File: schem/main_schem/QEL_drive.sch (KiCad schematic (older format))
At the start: 7 parts, among them P1 CONN_2, Q1 ENHANCED_MOSFET_N, U1 PS2501-2

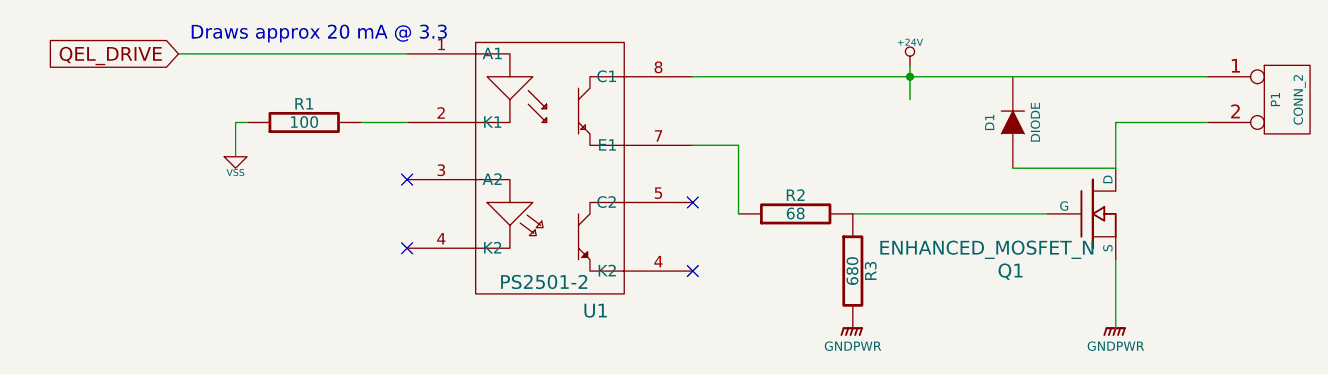
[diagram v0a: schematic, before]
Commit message: Begin board, layout mcu, xtal, eeprom
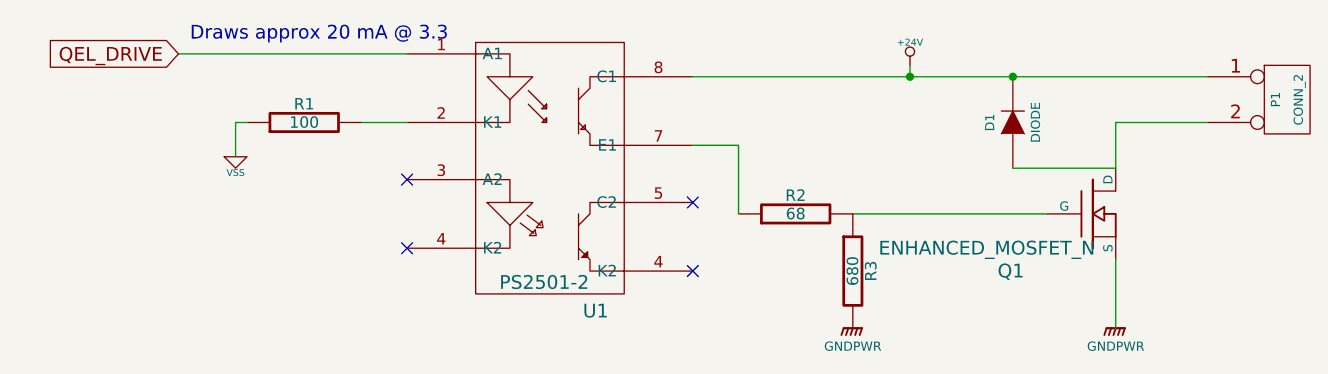
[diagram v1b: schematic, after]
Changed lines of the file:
@@
-EESchema Schematic File Version 2  date 9/29/2012 4:29:19 PM
+EESchema Schematic File Version 2  date 10/1/2012 7:44:23 AM
 LIBS:power
 LIBS:device
@@
 $Descr A4 11700 8267
 encoding utf-8
-Sheet 2 6
+Sheet 2 5
 Title "QEL_Driver"
-Date "29 sep 2012"
+Date "1 oct 2012"
 Rev "2"
 Comp "ECE 402 Senior Design"
@@
 $EndDescr
 Wire Wire Line
-	8150 4550 8150 4250
+	6300 3450 8550 3450
+Wire Wire Line
+	7250 3450 7250 3400
+Wire Wire Line
+	6500 4050 6500 3750
+Wire Wire Line
+	6500 3750 6300 3750
+Wire Wire Line
+	7700 3850 8150 3850
+Connection ~ 7250 3450
+Wire Wire Line
+	8550 3650 8150 3650
+Wire Wire Line
+	4300 3800 4300 3650
+Wire Wire Line
+	4300 3650 4350 3650
+Wire Wire Line
+	4050 3350 5050 3350
+Wire Wire Line
+	4850 3650 5050 3650
+Wire Wire Line
+	8150 3650 8150 3850
 Wire Wire Line
 	7000 4050 7850 4050
 Wire Wire Line
-	8150 3650 8150 3850
-Wire Wire Line
-	8550 3450 6300 3450
-Wire Wire Line
-	7250 3550 7250 3400
-Wire Wire Line
-	4850 3650 5050 3650
-Wire Wire Line
-	4050 3350 5050 3350
-Wire Wire Line
-	4350 3650 4300 3650
-Wire Wire Line
-	4300 3650 4300 3800
-Wire Wire Line
-	8150 3650 8550 3650
-Connection ~ 7250 3450
-Wire Wire Line
-	8150 3850 7700 3850
-Wire Wire Line
-	6300 3750 6500 3750
-Wire Wire Line
-	6500 3750 6500 4050
+	8150 4550 8150 4250
+Connection ~ 7700 3450
 $Comp
-L GNDPWR #PWR?
+L GNDPWR #PWR01
 U 1 1 506747B4
 P 8150 4550
-F 0 "#PWR?" H 8150 4600 40  0001 C CNN
+F 0 "#PWR01" H 8150 4600 40  0001 C CNN
 F 1 "GNDPWR" H 8150 4470 40  0000 C CNN
 	1    8150 4550
@@
 $EndComp
 $Comp
-L GNDPWR #PWR?
+L GNDPWR #PWR02
 U 1 1 506747A8
 P 7000 4550
-F 0 "#PWR?" H 7000 4600 40  0001 C CNN
+F 0 "#PWR02" H 7000 4600 40  0001 C CNN
 F 1 "GNDPWR" H 7000 4470 40  0000 C CNN
 	1    7000 4550
@@
 NoConn ~ 5050 3900
 $Comp
-L VSS #PWR1
+L VSS #PWR03
 U 1 1 50674779
 P 4300 3800
-F 0 "#PWR1" H 4300 3800 30  0001 C CNN
+F 0 "#PWR03" H 4300 3800 30  0001 C CNN
 F 1 "VSS" H 4300 3730 30  0000 C CNN
 	1    4300 3800
@@
 $EndComp
 $Comp
-L +24V #PWR3
+L +24V #PWR04
 U 1 1 504BA51D
 P 7250 3400
-F 0 "#PWR3" H 7250 3350 20  0001 C CNN
+F 0 "#PWR04" H 7250 3350 20  0001 C CNN
 F 1 "+24V" H 7250 3500 30  0000 C CNN
 	1    7250 3400

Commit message: Ethernet Anolog, breakout pins, SPI iface breakout for NFC
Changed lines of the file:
@@
-EESchema Schematic File Version 2  date 10/1/2012 7:44:23 AM
+EESchema Schematic File Version 2  date 10/5/2012 10:31:23 AM
 LIBS:power
 LIBS:device
@@
 $Descr A4 11700 8267
 encoding utf-8
-Sheet 2 5
+Sheet 3 6
 Title "QEL_Driver"
-Date "1 oct 2012"
+Date "5 oct 2012"
 Rev "2"
 Comp "ECE 402 Senior Design"
@@
 Comment4 ""
 $EndDescr
+Wire Wire Line
+	8150 4250 8150 4550
+Wire Wire Line
+	8150 3850 8150 3650
+Wire Wire Line
+	7850 4050 7000 4050
 Wire Wire Line
 	6300 3450 8550 3450
@@
 	6500 3750 6300 3750
 Wire Wire Line
-	7700 3850 8150 3850
+	8150 3850 7700 3850
 Connection ~ 7250 3450
 Wire Wire Line
-	8550 3650 8150 3650
+	8150 3650 8550 3650
 Wire Wire Line
 	4300 3800 4300 3650
@@
 Wire Wire Line
 	4850 3650 5050 3650
-Wire Wire Line
-	8150 3650 8150 3850
-Wire Wire Line
-	7000 4050 7850 4050
-Wire Wire Line
-	8150 4550 8150 4250
 Connection ~ 7700 3450
 $Comp

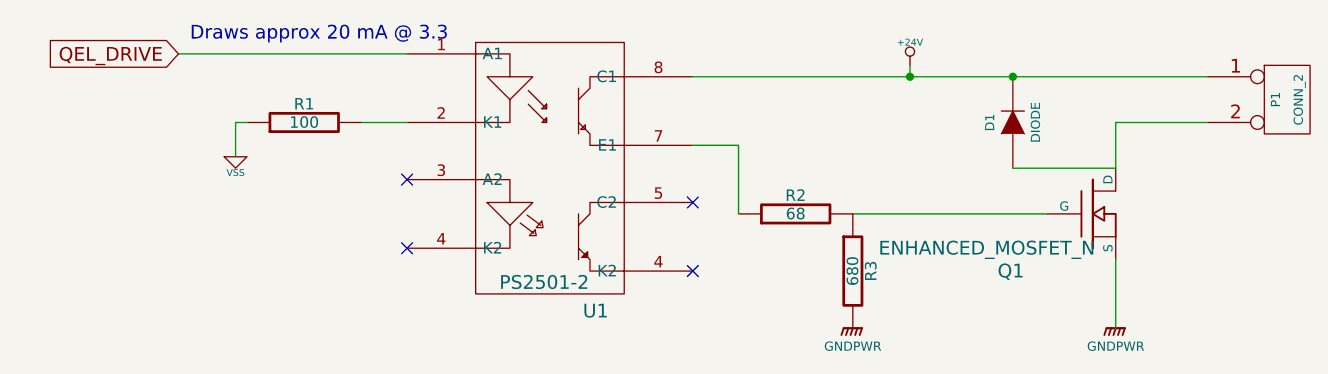
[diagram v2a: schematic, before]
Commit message: BOM sheets, update ethernet analog circuit
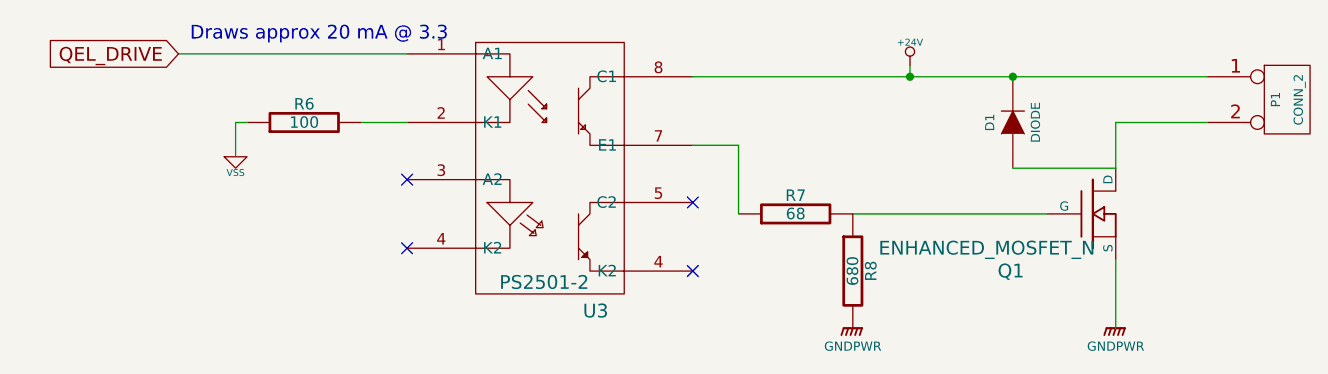
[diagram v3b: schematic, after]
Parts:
- renumbered R1 to R6, R2 to R7, R3 to R8, U1 to U3
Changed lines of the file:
@@
-EESchema Schematic File Version 2  date 10/5/2012 10:31:23 AM
+EESchema Schematic File Version 2  date 10/5/2012 11:52:46 PM
 LIBS:power
 LIBS:device
@@
 Sheet 3 6
 Title "QEL_Driver"
-Date "5 oct 2012"
+Date "6 oct 2012"
 Rev "2"
 Comp "ECE 402 Senior Design"
@@
 Connection ~ 7700 3450
 $Comp
-L GNDPWR #PWR01
+L GNDPWR #PWR08
 U 1 1 506747B4
 P 8150 4550
-F 0 "#PWR01" H 8150 4600 40  0001 C CNN
+F 0 "#PWR08" H 8150 4600 40  0001 C CNN
 F 1 "GNDPWR" H 8150 4470 40  0000 C CNN
 	1    8150 4550
@@
 $EndComp
 $Comp
-L GNDPWR #PWR02
+L GNDPWR #PWR09
 U 1 1 506747A8
 P 7000 4550
-F 0 "#PWR02" H 7000 4600 40  0001 C CNN
+F 0 "#PWR09" H 7000 4600 40  0001 C CNN
 F 1 "GNDPWR" H 7000 4470 40  0000 C CNN
 	1    7000 4550
@@
 NoConn ~ 5050 3900
 $Comp
-L VSS #PWR03
+L VSS #PWR010
 U 1 1 50674779
 P 4300 3800
-F 0 "#PWR03" H 4300 3800 30  0001 C CNN
+F 0 "#PWR010" H 4300 3800 30  0001 C CNN
 F 1 "VSS" H 4300 3730 30  0000 C CNN
 	1    4300 3800
@@
 $EndComp
 $Comp
-L R R2
+L R R7
 U 1 1 5058DB7E
 P 6750 4050
-F 0 "R2" V 6830 4050 50  0000 C CNN
+F 0 "R7" V 6830 4050 50  0000 C CNN
 F 1 "68" V 6750 4050 50  0000 C CNN
 	1    6750 4050
@@
 $EndComp
 $Comp
-L R R3
+L R R8
 U 1 1 5058DB66
 P 7000 4300
-F 0 "R3" V 7080 4300 50  0000 C CNN
+F 0 "R8" V 7080 4300 50  0000 C CNN
 F 1 "680" V 7000 4300 50  0000 C CNN
 	1    7000 4300
@@
 $EndComp
 $Comp
-L +24V #PWR04
+L +24V #PWR011
 U 1 1 504BA51D
 P 7250 3400
-F 0 "#PWR04" H 7250 3350 20  0001 C CNN
+F 0 "#PWR011" H 7250 3350 20  0001 C CNN
 F 1 "+24V" H 7250 3500 30  0000 C CNN
 	1    7250 3400
@@
 Draws approx 20 mA @ 3.3
 $Comp
-L R R1
+L R R6
 U 1 1 504B9FF4
 P 4600 3650
-F 0 "R1" V 4680 3650 50  0000 C CNN
+F 0 "R6" V 4680 3650 50  0000 C CNN
 F 1 "100" V 4600 3650 50  0000 C CNN
 	1    4600 3650
@@
 QEL_DRIVE
 $Comp
-L PS2501-2 U1
+L PS2501-2 U3
 U 1 1 504B9FB2
 P 5700 3550
-F 0 "U1" H 5875 2625 60  0000 C CNN
+F 0 "U3" H 5875 2625 60  0000 C CNN
 F 1 "PS2501-2" H 5650 2750 60  0000 C CNN
 	1    5700 3550

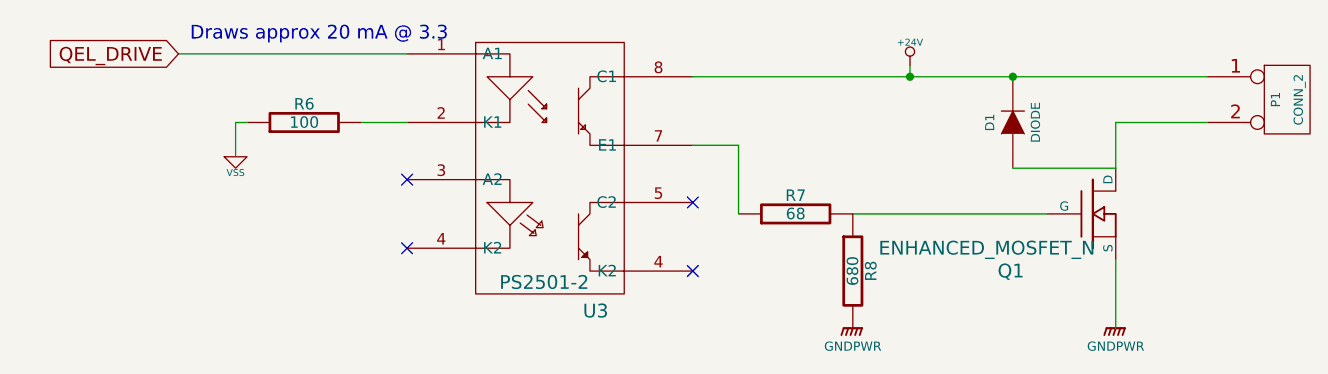
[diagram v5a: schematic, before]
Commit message: Change opto-isolator to ps2501-1 style
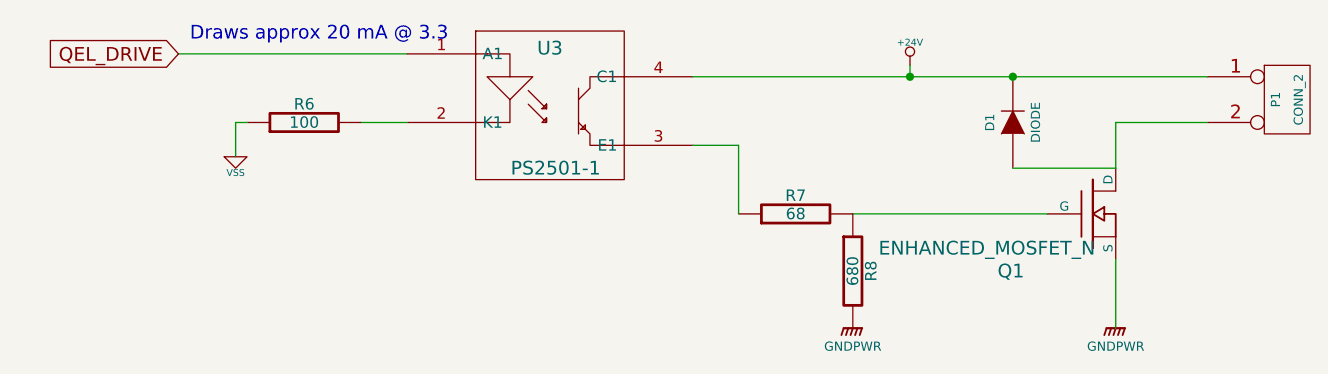
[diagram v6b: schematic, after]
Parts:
- removed U3: PS2501-2, symbol PS2501-2
- added U3: PS2501-1, symbol PS2501-1
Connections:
- net +24V: now also U3.4 (C1)
- net QEL_DRIVE: now also U3.1 (A1)
- net at R6.2: now also U3.2 (K1)
- net at R7.1: now also U3.3 (NC)
- no-connect marks 4 -> 0
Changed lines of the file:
@@
-EESchema Schematic File Version 2  date 10/7/2012 8:27:40 PM
+EESchema Schematic File Version 2  date 10/7/2012 9:06:12 PM
 LIBS:power
 LIBS:device
@@
 Comment4 ""
 $EndDescr
+$Comp
+L PS2501-1 U3
+U 1 1 5072317B
+P 5700 3550
+F 0 "U3" H 5675 3775 60  0000 C CNN
+F 1 "PS2501-1" H 5700 3250 60  0000 C CNN
+	1    5700 3550
+	1    0    0    -1
+$EndComp
 Wire Wire Line
 	8150 4250 8150 4550
@@
 	1    0    0    -1
 $EndComp
-NoConn ~ 6300 4300
-NoConn ~ 6300 4000
-NoConn ~ 5050 4200
-NoConn ~ 5050 3900
 $Comp
 L VSS #PWR010
@@
 Text GLabel 4050 3350 0    60   Input ~ 0
 QEL_DRIVE
-$Comp
-L PS2501-2 U3
-U 1 1 504B9FB2
-P 5700 3550
-F 0 "U3" H 5875 2625 60  0000 C CNN
-F 1 "PS2501-2" H 5650 2750 60  0000 C CNN
-	1    5700 3550
-	1    0    0    -1
-$EndComp
 $EndSCHEMATC
